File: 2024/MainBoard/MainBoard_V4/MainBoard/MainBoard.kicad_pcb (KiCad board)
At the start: 2 copper layers, 115.8 x 60.5 mm, 88 parts, among them J1 Raspberry_Pi_2_3, J11 ADC2, J12 ADC2, J13 Drib, J14 UART, J15 TFT3, J16 CAN_CON, J2 fan, J3 USB_C_Receptacle_USB2.0_16P, J5 MOLEX MINISPOX, J6 Debug, J7 ADC0, Q1 NMOS, Q2 PMOS, Q3 PMOS, SW1 SW_MEC_5E, SW4 SW_Wuerth_450301014042, SW5 Ras_1, SW6 Ras_2, U1 STM32F446RETx, U2 CH340E, U3 MOUDLE-SEEEDUINO-XIAO, U7 AZ1117-3.3, U8 MAX3051, Y1 CSTNE16M0V530000R0

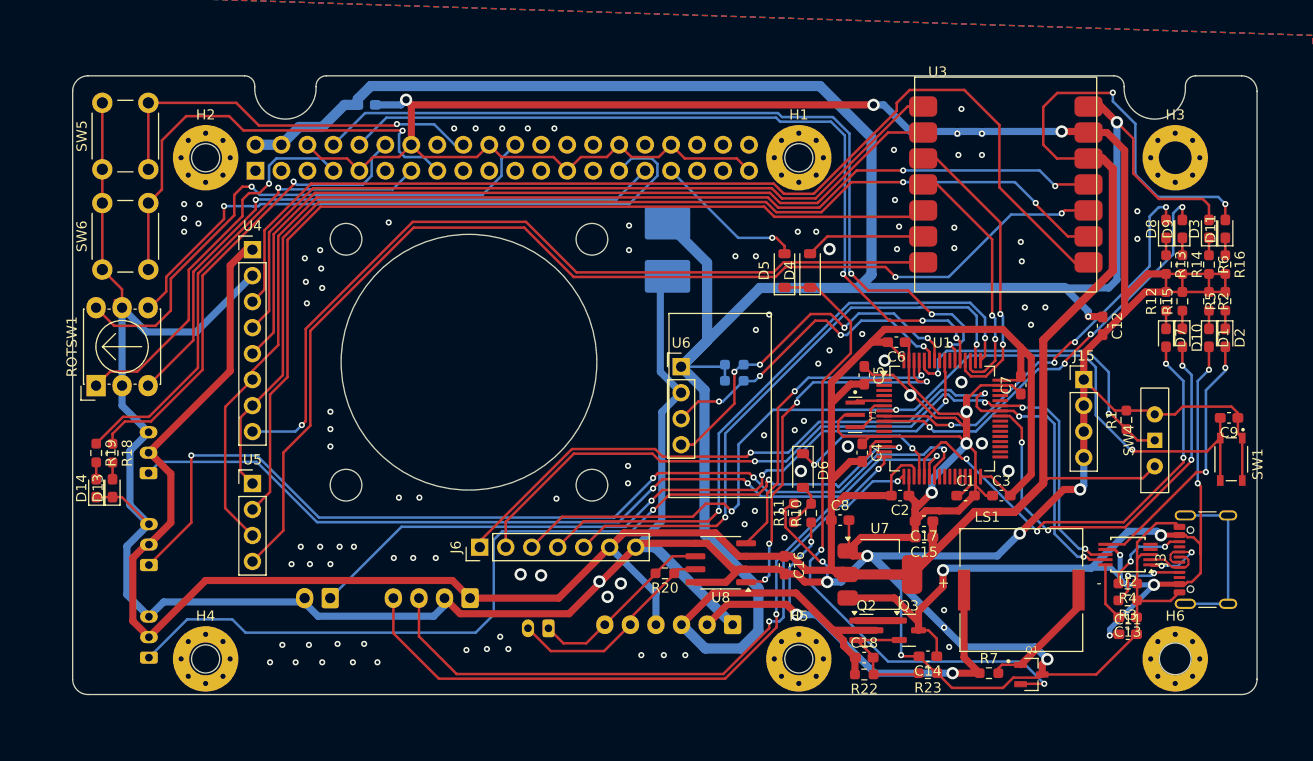
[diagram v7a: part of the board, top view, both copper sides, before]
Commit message: ✨レビューしたよ
- CANBUSのアートワークの修正
- トランシーバの位置を変更

- ビアを打った
- CANトランシーバの位置変更に伴い配線の変更をした
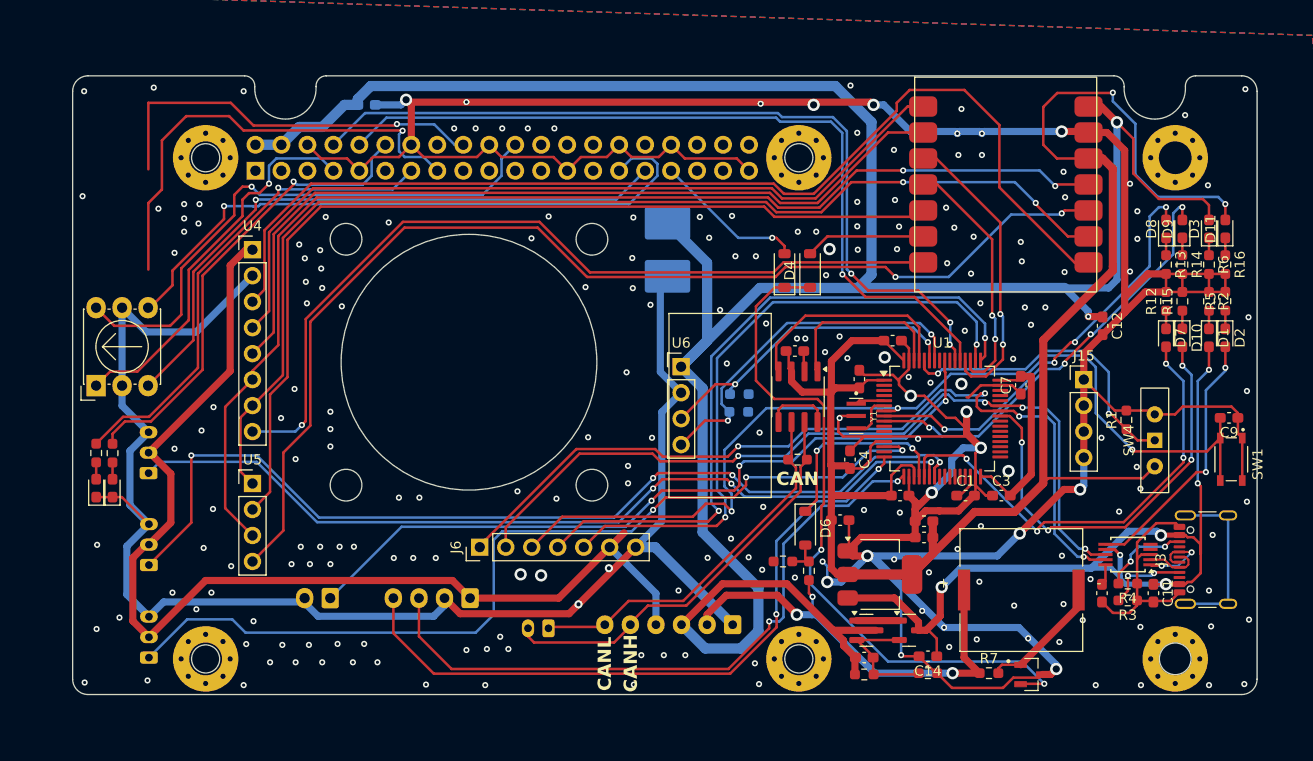
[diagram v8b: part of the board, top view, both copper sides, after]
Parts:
- removed SW5: Ras_1, Button_Switch_THT:SW_PUSH_6mm_H7.3mm
- removed SW6: Ras_2, Button_Switch_THT:SW_PUSH_6mm_H7.3mm
- moved C16 21.0 mm to (7.32, -5.33), turned to 0 degrees
- moved U8 17.9 mm to (7.62, -0.86), turned to -90 degrees
- moved R20 17.1 mm to (7.57, 5.28)
- moved R10 5.65 mm to (8.69, 16.2)
- moved D6 5.64 mm to (8.33, 12.0)
- moved R11 4.87 mm to (6.14, 15.2), turned to 180 degrees
- moved C11 4.74 mm to (42.4, 18.3), turned to -90 degrees
- moved R9 4.63 mm to (1.83, 0.61), turned to 0 degrees
- moved C13 3.45 mm to (37.3, 18.3), turned to 90 degrees
- moved R8 1.40 mm to (1.88, -1.12), turned to 0 degrees
- moved C4 1.38 mm to (12.7, 5.28)
- moved C5 0.61 mm to (13.6, -2.59)
- moved C6 0.40 mm to (16.9, -6.35)
- moved Y1 0.15 mm to (13.3, 1.02)
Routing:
- net GND: track 637.3 -> 579.5 mm, vias 116 -> 220
- net +3.3V: track 340.0 -> 304.1 mm
- net CANH: track 21.4 -> 42.0 mm
- net CAN1_TX: track 37.5 -> 17.3 mm, vias 4 -> 0
- net CANL: track 18.5 -> 36.8 mm
- net CAN1_RX: track 31.4 -> 21.6 mm, vias 2 -> 0
- net +5VL: track 93.8 -> 86.8 mm, vias 7 -> 6
- net SWDIO: track 57.7 -> 63.2 mm
- net SWCLK: track 61.1 -> 66.6 mm
- net VD: track 49.2 -> 44.9 mm
- net +5V: track 256.3 -> 252.0 mm
- net Net-(D4-K): track 64.4 -> 68.2 mm
- net Net-(U2-V3): track 5.68 -> 2.05 mm
- net BATTERY_MEASURE: track 15.9 -> 19.3 mm
- net Ras_TX: track 84.1 -> 82.0 mm
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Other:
- board text added: "CAN"
- board text added: "CANH"
- board text added: "CANL"
